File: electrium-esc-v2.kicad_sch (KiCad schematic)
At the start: 4 parts

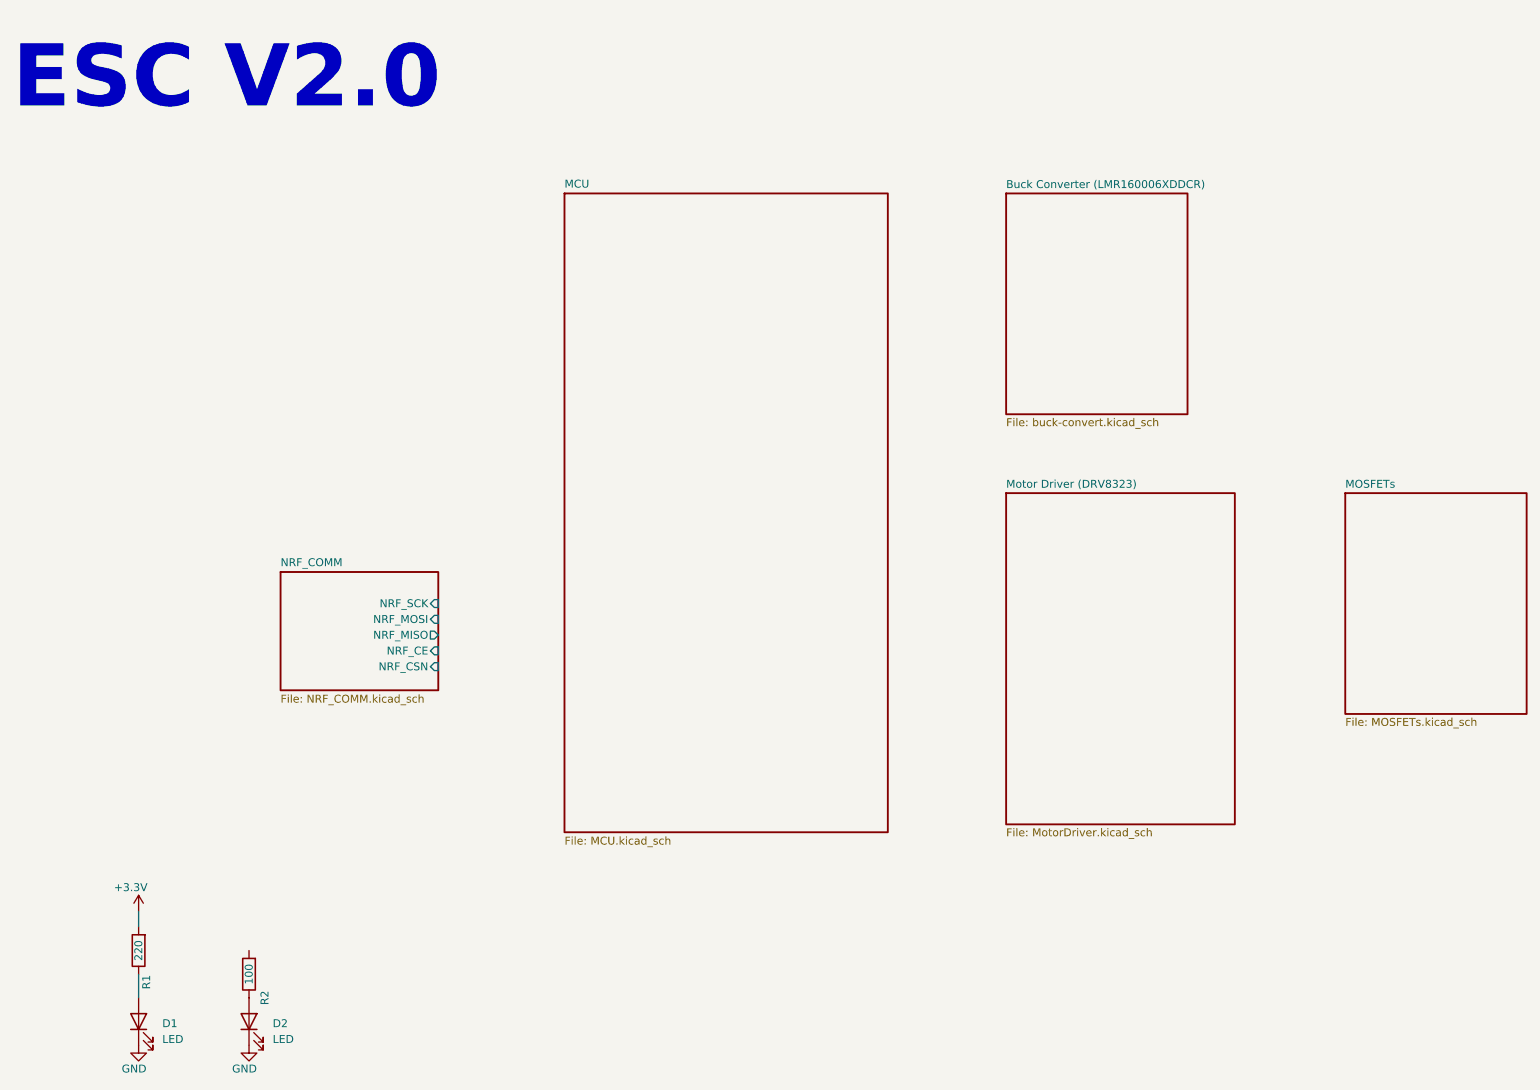
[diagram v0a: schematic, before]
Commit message: Remove dup folder
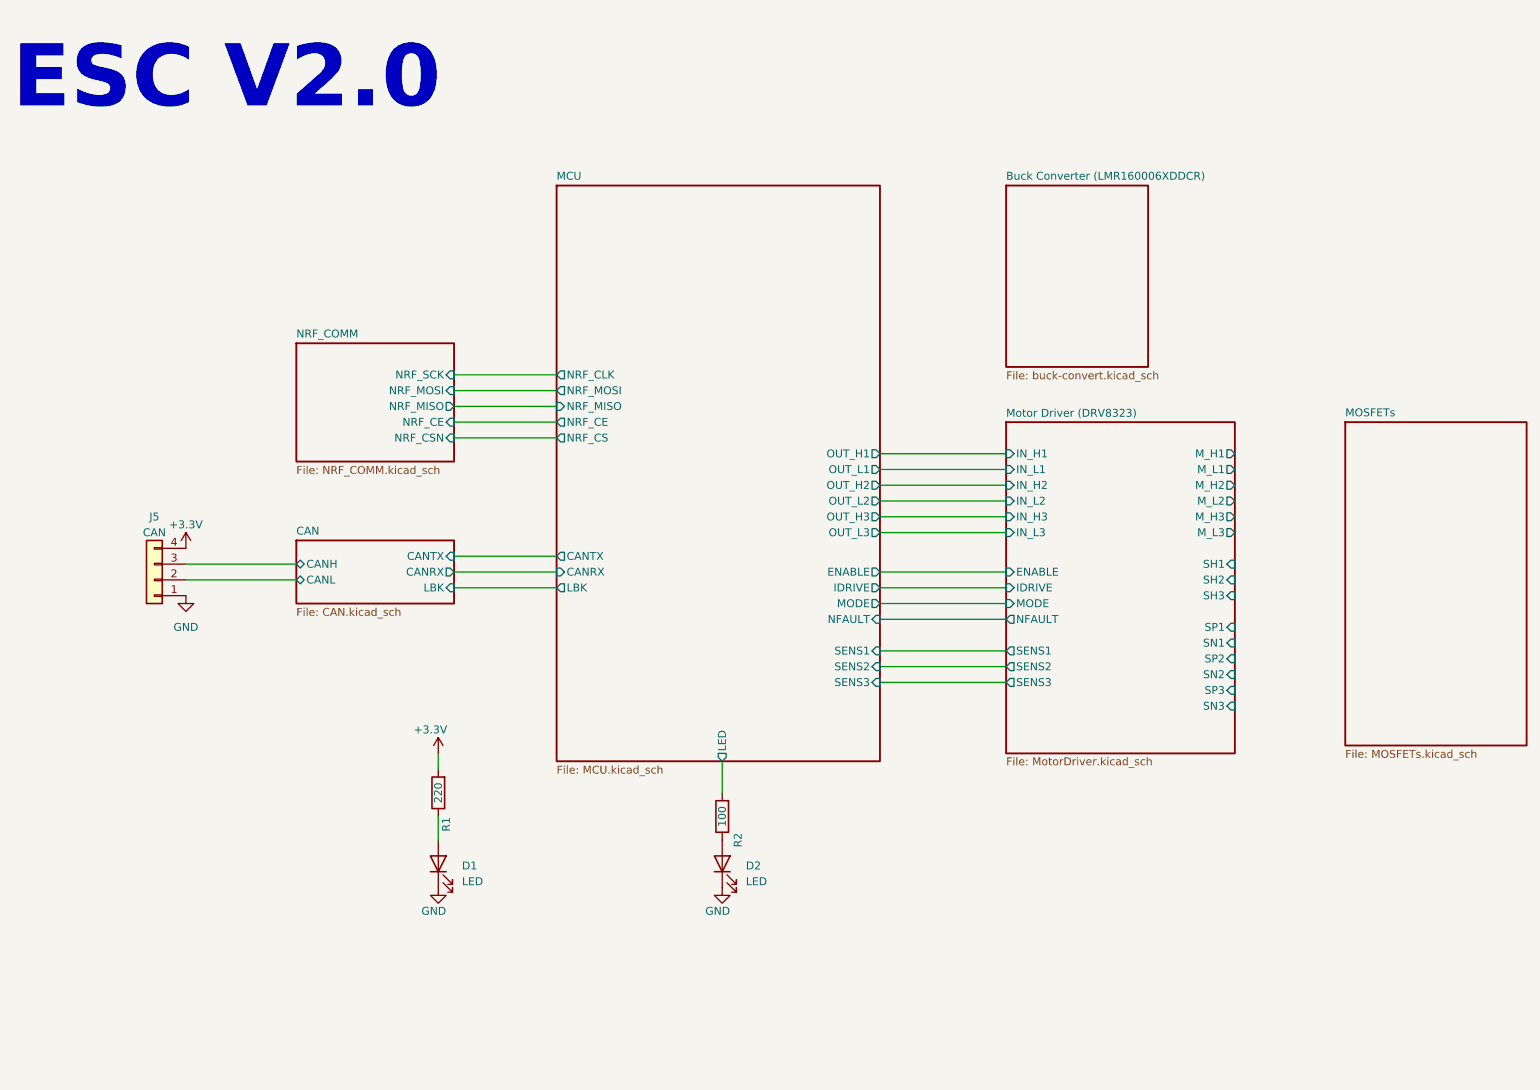
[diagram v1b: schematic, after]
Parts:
- added J5: CAN, symbol Connector_Generic:Conn_01x04
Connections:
- net +3.3V: now also J5.4 (Pin_4)
- net GND: now also J5.1 (Pin_1)
- net MCU/LED: now reaches R2.2
- new net CAN/CANH: J5.3 (Pin_3)
- new net CAN/CANL: J5.2 (Pin_2)
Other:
- added sheet CAN (CAN.kicad_sch)
- sheet MCU ports: added CANRX, CANTX, ENABLE, IDRIVE, LBK, LED, MODE, NFAULT, NRF_CE, NRF_CLK, NRF_CS, NRF_MISO, NRF_MOSI, OUT_H1, OUT_H2, OUT_H3, OUT_L1, OUT_L2, OUT_L3, SENS1, SENS2, SENS3; removed none
- sheet Motor Driver (DRV8323) ports: added ENABLE, IDRIVE, IN_H1, IN_H2, IN_H3, IN_L1, IN_L2, IN_L3, MODE, M_H1, M_H2, M_H3, M_L1, M_L2, M_L3, NFAULT, SENS1, SENS2, SENS3, SH1, SH2, SH3, SN1, SN2, SN3, SP1, SP2, SP3; removed none
- moved on the sheet: D1, D2, R1, R2

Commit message: Additional renaming
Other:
- sheet Buck Converter (LMR160006XDDCR) renamed Buck Converter (LMR36510FADDAR)
- sheet MCU renamed MCU (RP2040)
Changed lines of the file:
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@@
     (stroke (width 0.3) (type solid))
     (fill (color 0 0 0 0.0000))
-    (property "Sheetname" "MCU" (at 107.95 43.6646 0)
+    (property "Sheetname" "MCU (RP2040)" (at 107.95 43.6646 0)
       (effects (font (size 1.27 1.27)) (justify left bottom))
     )
@@
     (stroke (width 0.3) (type solid))
     (fill (color 0 0 0 0.0000))
-    (property "Sheetname" "Buck Converter (LMR160006XDDCR)" (at 180.34 43.6646 0)
-      (effects (font (size 1.27 1.27)) (justify left bottom))
-    )
+    (property "Sheetname" "Buck Converter (LMR36510FADDAR)" (at 180.34 43.6646 0)
+      (effects (font (size 1.27 1.27)) (justify left bottom))
+    )
